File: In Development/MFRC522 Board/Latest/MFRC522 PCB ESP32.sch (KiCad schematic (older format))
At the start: 48 parts, among them P1 ESP32 NODEMCU DEVKIT1 LEFT HE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, P2 ESP32 NODEMCU DEVKIT1 RIGHT H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, Q2 Q_NPN_BEC, U1 MFRC522, Y1 27.12 MHz

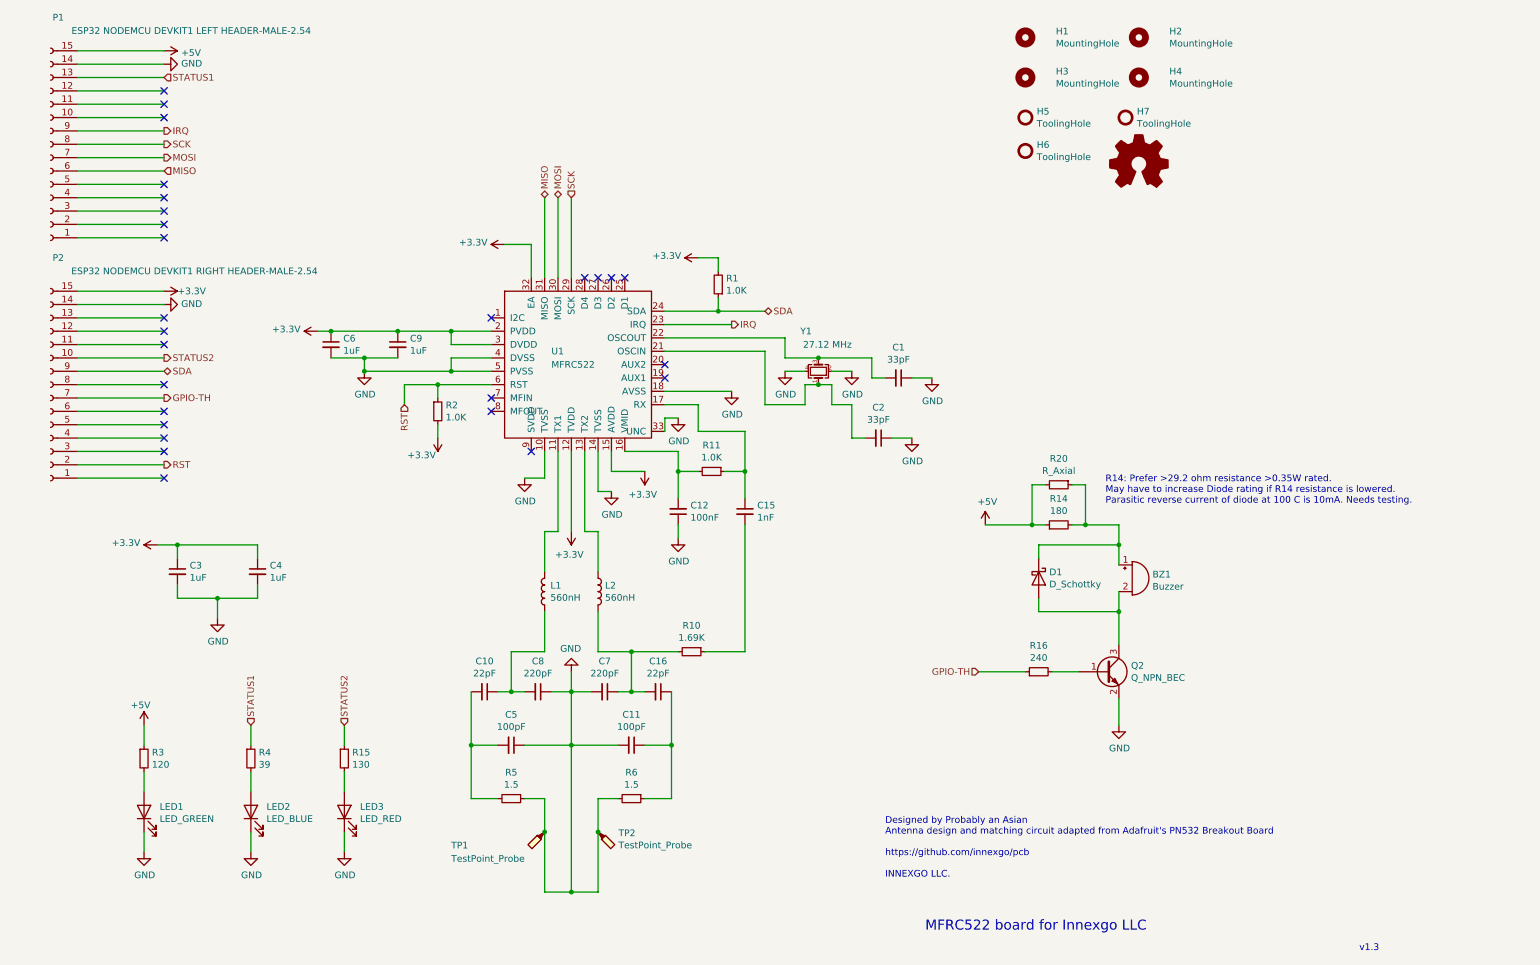
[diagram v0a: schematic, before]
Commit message: placement updated
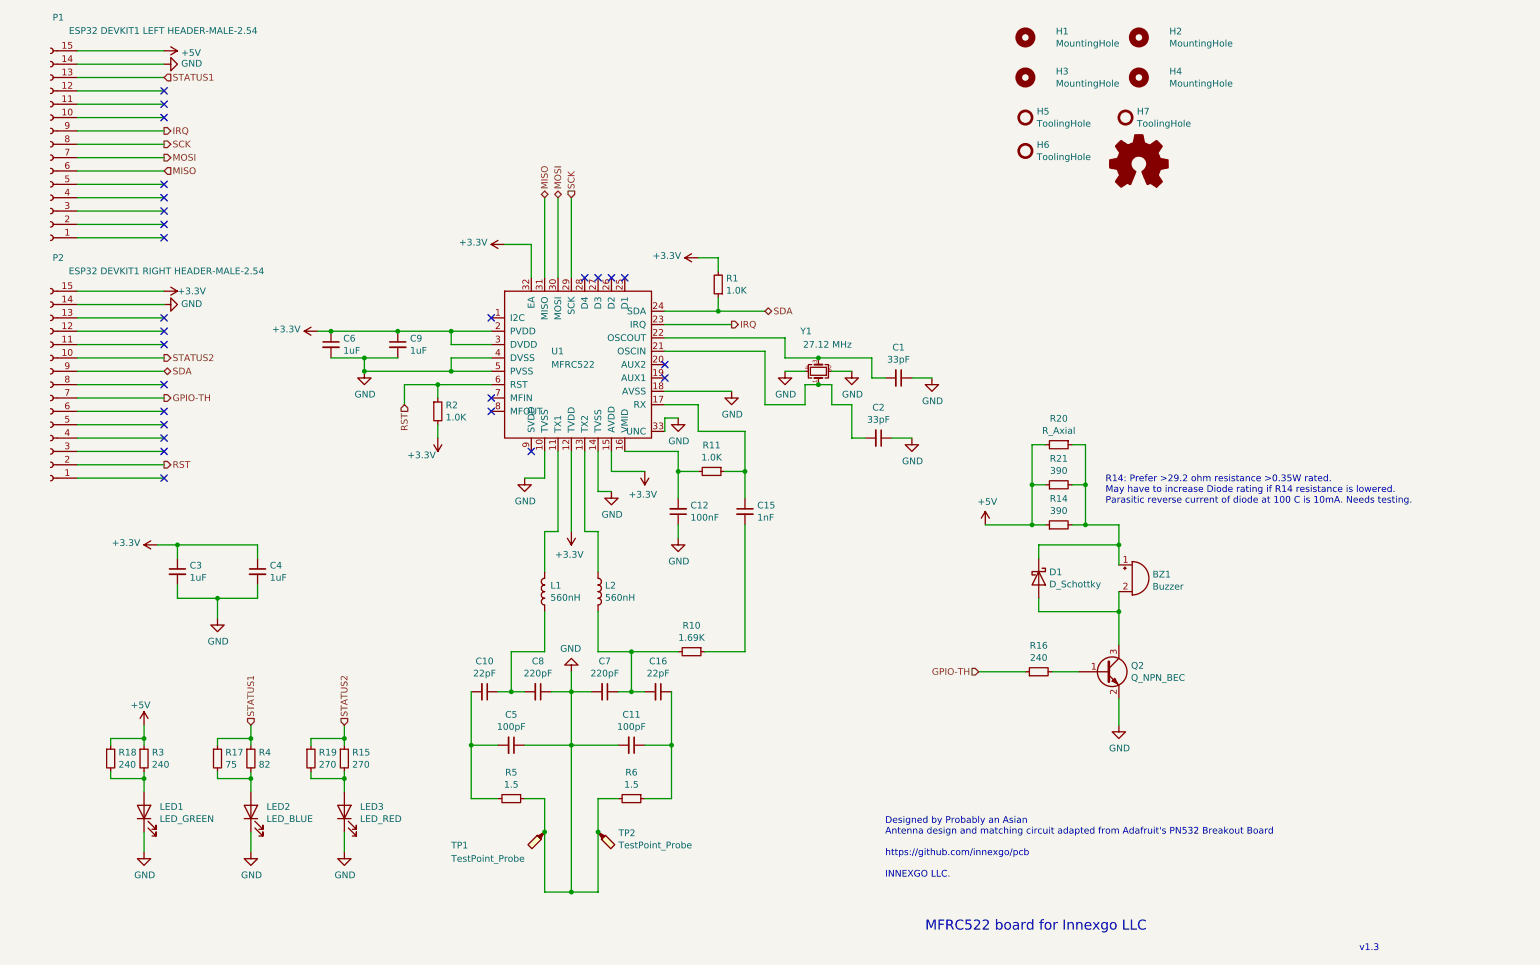
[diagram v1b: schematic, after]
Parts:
- added R17: 75, Resistor_SMD:R_0603_1608Metric, symbol Device:R_Small
- added R18: 240, Resistor_SMD:R_0603_1608Metric, symbol Device:R_Small
- added R19: 270, Resistor_SMD:R_0603_1608Metric, symbol Device:R_Small
- added R21: 390, Resistor_SMD:R_0805_2012Metric, symbol Device:R_Small
- D1: LCSC Part (none) -> C2480
- LED1: LCSC Part (none) -> C72043
- LED2: LCSC Part (none) -> C72041
- LED3: footprint LED_SMD:LED_0603_1608Metric -> LED_SMD:LED_0805_2012Metric; LCSC Part (none) -> C84256
- P1: value ESP32 NODEMCU DEVKIT1 LEFT HEADER-MALE-2.54 -> ESP32 DEVKIT1 LEFT HEADER-MALE-2.54
- P2: value ESP32 NODEMCU DEVKIT1 RIGHT HEADER-MALE-2.54 -> ESP32 DEVKIT1 RIGHT HEADER-MALE-2.54
- Q2: LCSC Part (none) -> C2150
- R14: value 180 -> 390; footprint Resistor_SMD:R_2010_5025Metric -> Resistor_SMD:R_0805_2012Metric
- R15: value 130 -> 270
- R3: value 120 -> 240
- R4: value 39 -> 82
- U1: LCSC Part (none) -> C11322
- Y1: LCSC Part (none) -> C164053
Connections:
- net +5V: now also R18.1, R21.1
- net STATUS1: now also R17.1
- net STATUS2: now also R19.1
- net at LED1.2 (A), R3.2: now also R18.2
- net at LED2.2 (A), R4.2: now also R17.2
- net at BZ1.1 (-), D1.1 (K), R14.2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: now also R21.2
- net at LED3.2 (A), R15.2: now also R19.2
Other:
- moved on the sheet: R20

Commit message: more edits`
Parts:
- BZ1: footprint Buzzer_Beeper:Buzzer_12x9.5RM6.5 -> Custom:8.5mm_8.5mm_MLT_8530_BUZZER
- R14, R21: value 390 -> 220
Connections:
- net +3V3: now also R14.1, R20.2, R21.1
- net +5V: no longer R14.1, R20.2, R21.1
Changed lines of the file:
@@
 F 0 "BZ1" H 9052 4879 50  0000 L CNN
 F 1 "Buzzer" H 9052 4788 50  0000 L CNN
-F 2 "Buzzer_Beeper:Buzzer_12x9.5RM6.5" V 8875 4950 50  0001 C CNN
+F 2 "Custom:8.5mm_8.5mm_MLT_8530_BUZZER" V 8875 4950 50  0001 C CNN
 F 3 "~" V 8875 4950 50  0001 C CNN
 	1    8900 4850
@@
 F 3 "" H 8800 5950 50  0001 C CNN
 	1    8800 5950
-	1    0    0    -1
-$EndComp
-$Comp
-L power:+5V #PWR0129
-U 1 1 5EECE706
-P 7800 4450
-F 0 "#PWR0129" H 7800 4300 50  0001 C CNN
-F 1 "+5V" H 7815 4623 50  0000 C CNN
-F 2 "" H 7800 4450 50  0001 C CNN
-F 3 "" H 7800 4450 50  0001 C CNN
-	1    7800 4450
 	1    0    0    -1
 $EndComp
@@
 P 8350 4450
 F 0 "R14" V 8546 4450 50  0000 C CNN
-F 1 "390" V 8455 4450 50  0000 C CNN
+F 1 "220" V 8455 4450 50  0000 C CNN
 F 2 "Resistor_SMD:R_0805_2012Metric" H 8350 4450 50  0001 C CNN
 F 3 "~" H 8350 4450 50  0001 C CNN
@@
 Wire Wire Line
 	6550 3200 6950 3200
-Text Notes 8700 4300 0    50   ~ 0
-R14: Prefer >29.2 ohm resistance >0.35W rated.\nMay have to increase Diode rating if R14 resistance is lowered.\nParasitic reverse current of diode at 100 C is 10mA. Needs testing.
 Wire Wire Line
 	5800 2750 5800 2850
@@
 P 8350 4150
 F 0 "R21" V 8546 4150 50  0000 C CNN
-F 1 "390" V 8455 4150 50  0000 C CNN
+F 1 "220" V 8455 4150 50  0000 C CNN
 F 2 "Resistor_SMD:R_0805_2012Metric" H 8350 4150 50  0001 C CNN
 F 3 "~" H 8350 4150 50  0001 C CNN
@@
 Wire Wire Line
 	8150 4150 8150 4450
+$Comp
+L power:+3.3V #PWR0125
+U 1 1 608A03BF
+P 7800 4300
+F 0 "#PWR0125" H 7800 4150 50  0001 C CNN
+F 1 "+3.3V" H 7815 4473 50  0000 C CNN
+F 2 "" H 7800 4300 50  0001 C CNN
+F 3 "" H 7800 4300 50  0001 C CNN
+	1    7800 4300
+	1    0    0    -1
+$EndComp
+Wire Wire Line
+	7800 4450 7800 4300
+Text Notes 8700 4300 0    50   ~ 0
+R14: Prefer >29.2 ohm resistance >0.35W rated.\nMay have to increase Diode rating if R14 resistance is lowered.\nParasitic reverse current of diode at 100 C is 10mA. Needs testing.
 $EndSCHEMATC
